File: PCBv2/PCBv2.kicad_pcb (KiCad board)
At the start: 2 copper layers, 150 x 110 mm, 76 parts, among them IC1 MAX743CWE+, J1 Arduino_Mega_Header, J10 Screw_Terminal_01x03, J11 Screw_Terminal_01x03, J12 Screw_Terminal_01x03, J13 Screw_Terminal_01x03, J2 Conn_01x10, J3 Conn_01x08, J4 Conn_01x08, J5 Conn_02x18_Odd_Even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

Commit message: Added photos of the prototype and changed the PCB
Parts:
- removed C20: 100nF, Cap:Cap
- moved C19 16.8 mm to (119.3, 144.0), turned to 270 degrees
- moved U3 14.9 mm to (173.1, 55.5)
- moved J13 14.6 mm to (213.8, 141.8)
- moved J12 14.5 mm to (213.8, 126.2)
- moved J11 14.4 mm to (213.8, 110.8)
- moved J10 14.4 mm to (213.7, 95.3)
- moved J9 14.2 mm to (213.7, 80.0)
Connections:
- C19 pad 2: /-15V -> /5V
- D5 pad 1: Net-(D5-Pad1) -> /5V
- R20 pad 2: Net-(D5-Pad1) -> /5V
- R21 pad 2: Net-(D5-Pad1) -> /5V
- U10 pad 4: /-15V -> /GND
- U10 pad 8: /+15V -> /5V
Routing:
- net /5V: track 205.5 -> 340.5 mm, vias 4 -> 7
- net /PIN50: track 192.9 -> 208.8 mm
- net /PIN53: track 25.2 -> 40.8 mm
- net /SMU2: track 102.7 -> 117.7 mm
- net /PIN51: track 23.7 -> 38.6 mm
- net /PIN52: track 186.8 -> 201.7 mm
- net /E-AMPLI: track 18.2 -> 33.0 mm
- net /E4: track 28.5 -> 43.1 mm
- net /E7: track 23.8 -> 38.4 mm
- net /SMU-IN: track 17.0 -> 31.5 mm
- net /E8: track 22.0 -> 36.5 mm
- net /E6: track 25.8 -> 40.3 mm
- net /E5: track 27.0 -> 41.5 mm
- net /ARDU-A11: track 103.4 -> 117.8 mm
- net /ARDU-A9: track 105.2 -> 119.5 mm
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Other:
- board size 150 x 110 mm -> 165.1 x 110 mm

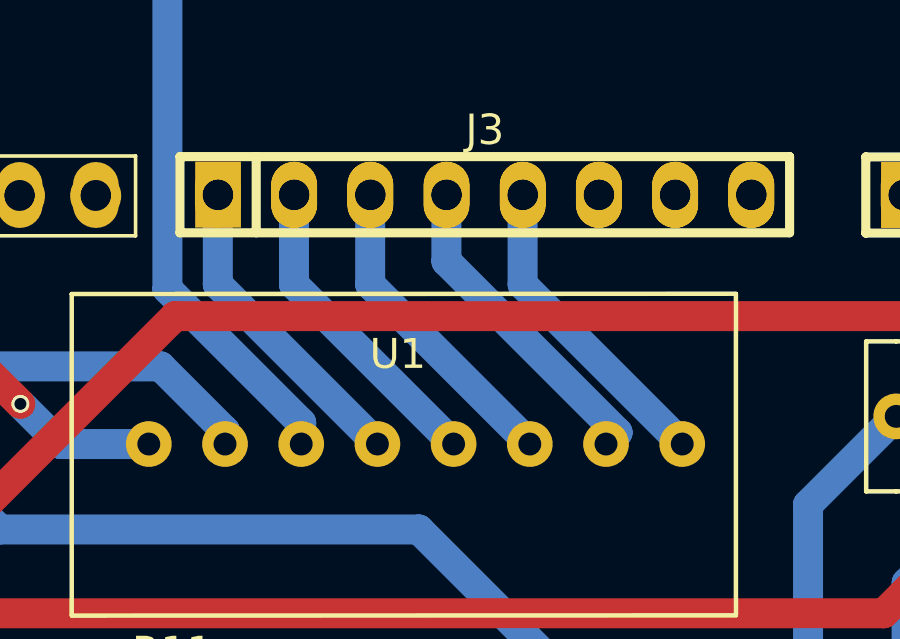
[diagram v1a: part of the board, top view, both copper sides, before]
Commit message: Changes on PCB and pins of LCD
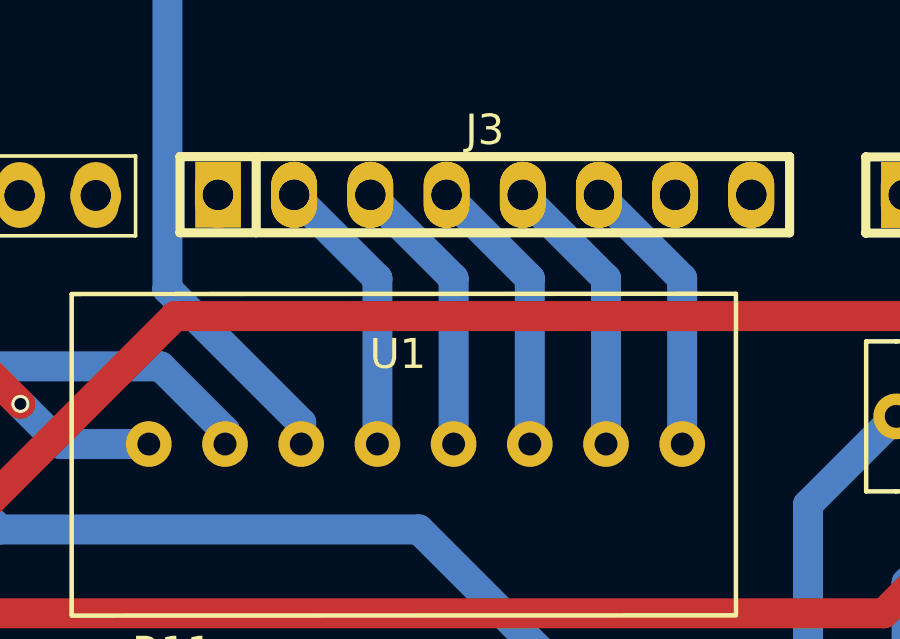
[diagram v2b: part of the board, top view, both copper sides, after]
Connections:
- J1 pad 71: Net-(J1-Pad71) -> /PIN2
- J1 pad 76: /PIN7 -> Net-(J1-Pad76)
- J3 pad 1: /PIN7 -> Net-(J3-Pad1)
- J3 pad 6: Net-(J3-Pad6) -> /PIN2
- U1 pad 1: /PIN3 -> /PIN2
- U1 pad 2: /PIN4 -> /PIN3
- U1 pad 3: /PIN5 -> /PIN4
- U1 pad 4: /PIN6 -> /PIN5
- U1 pad 5: /PIN7 -> /PIN6
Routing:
- net /PIN7: track 10.5 -> 0.00 mm
- net /PIN2: track 0.00 -> 9.45 mm
- net /PIN4: track 10.8 -> 9.45 mm
- net /PIN5: track 10.5 -> 9.45 mm
- net /PIN3: track 10.5 -> 9.45 mm
- net /PIN6: track 10.5 -> 9.45 mm

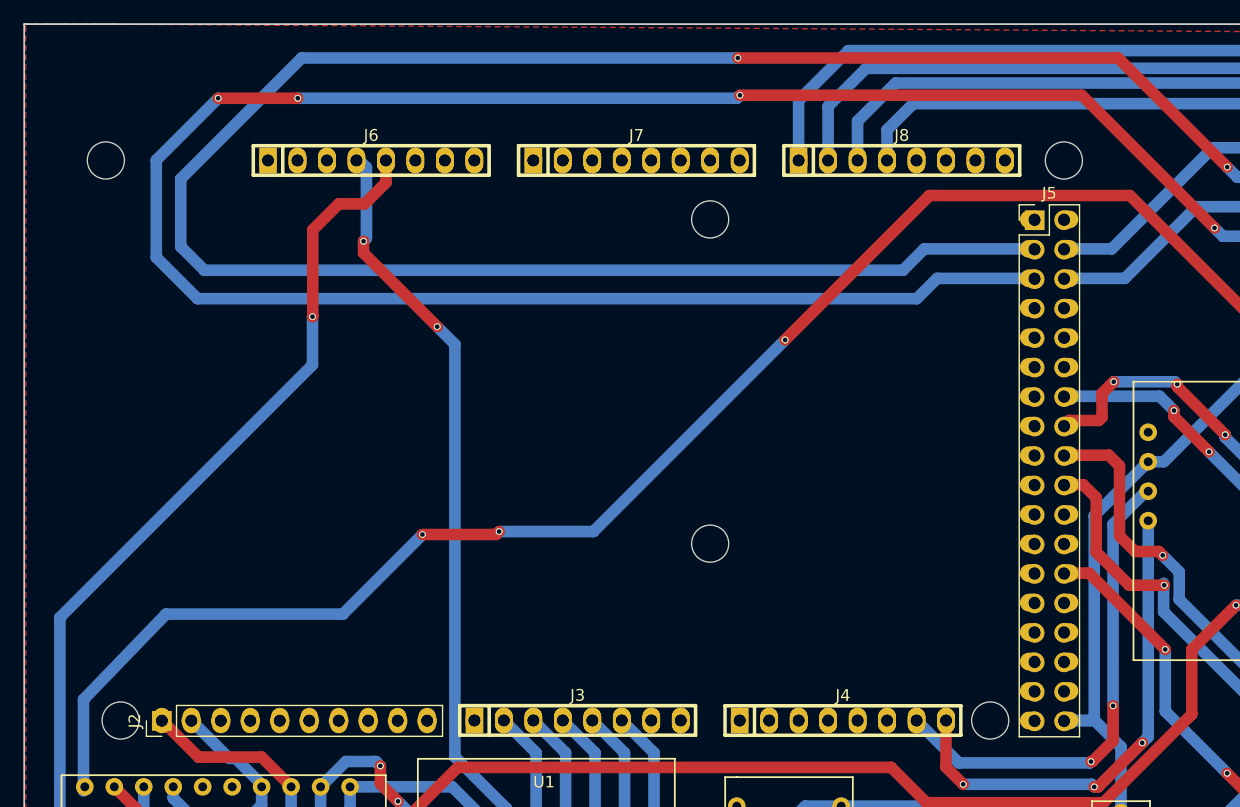
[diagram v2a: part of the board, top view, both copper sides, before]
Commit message: Added GPRS communications and lots of changes on the main code!
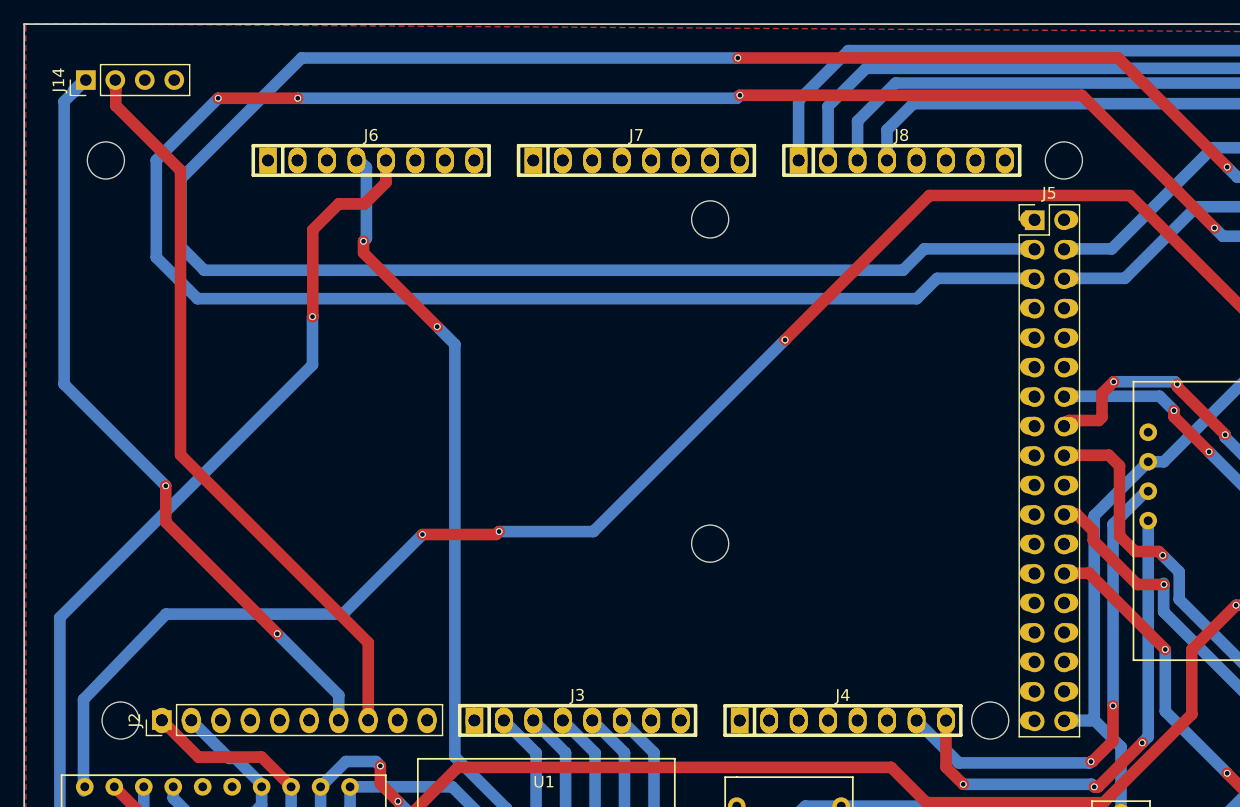
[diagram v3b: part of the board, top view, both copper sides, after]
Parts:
- added J14: Conn_01x04, Pin_Headers:Pin_Header_Straight_1x04_Pitch2.54mm, F.Cu at (55.3, 54.8)
- moved J2 0.07 mm to (61.9, 110.0)
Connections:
- J1 pad 52: /PIN37 -> Net-(J1-Pad52)
- J1 pad 53: Net-(J1-Pad53) -> /PIN35
- J1 pad 79: Net-(J1-Pad79) -> /PIN10
- J1 pad 80: Net-(J1-Pad80) -> /PIN11
- J2 pad 7: Net-(J2-Pad7) -> /PIN11
- J2 pad 8: Net-(J2-Pad8) -> /PIN10
- J5 pad 20: /PIN37 -> Net-(J5-Pad20)
- J5 pad 22: Net-(J5-Pad22) -> /PIN35
- U4 pad 2: /PIN37 -> /PIN35
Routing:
- net /PIN11: track 0.00 -> 67.4 mm, vias 0 -> 2
- net /PIN10: track 0.00 -> 65.8 mm
- net /PIN37: track 41.3 -> 0.00 mm, vias 3 -> 0
- net /PIN35: track 0.00 -> 38.7 mm, vias 0 -> 3

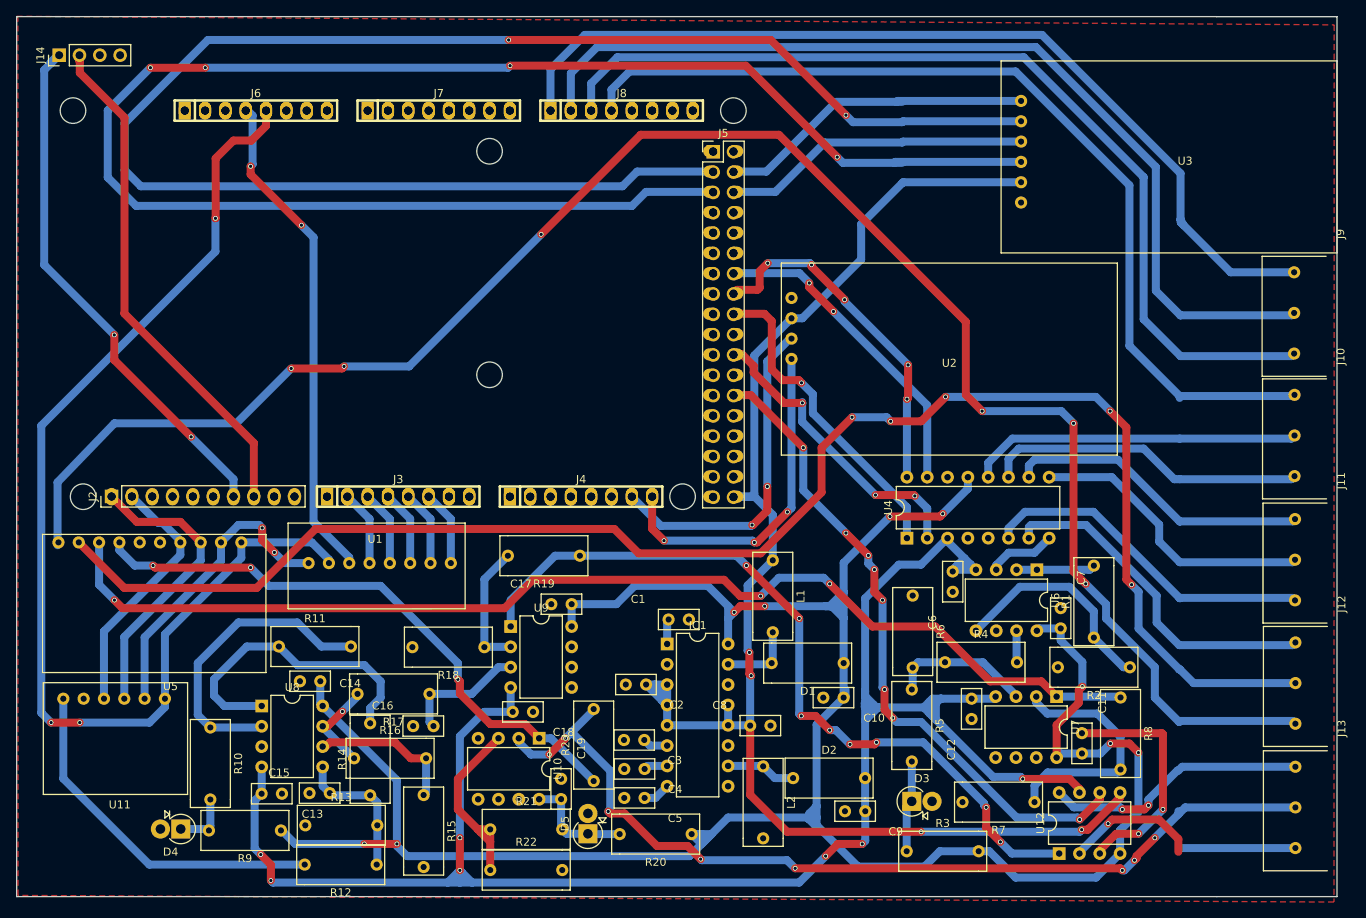
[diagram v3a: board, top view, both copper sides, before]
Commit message: Added pwr pin of the SIM900 and documentation made
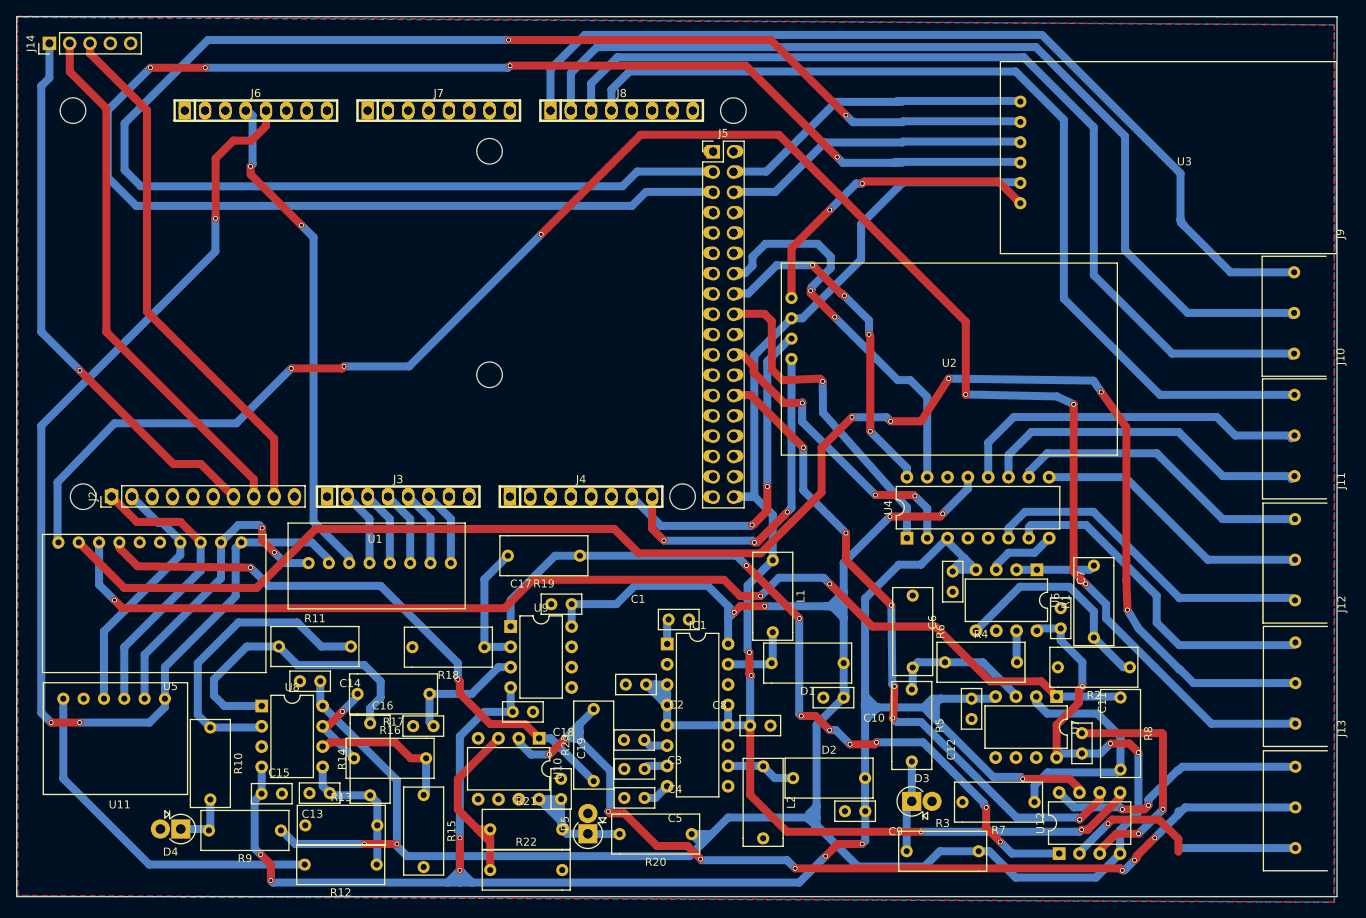
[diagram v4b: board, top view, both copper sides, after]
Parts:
- J14: value Conn_01x04 -> Conn_01x05; footprint Pin_Headers:Pin_Header_Straight_1x04_Pitch2.54mm -> Pin_Headers:Pin_Header_Straight_1x05_Pitch2.54mm
- moved J14 1.92 mm to (54.1, 53.3)
- moved U3 0.12 mm to (173.0, 55.6)
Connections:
- J1 pad 78: Net-(J1-Pad78) -> /PIN9
- J14 pad 3: /GND -> /PIN9
- J2 pad 9: Net-(J2-Pad9) -> /PIN9
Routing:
- net /PIN9: track 0.00 -> 66.2 mm
- net /GND: track 68.2 -> 107.6 mm, vias 4 -> 6
- net /PIN43: track 40.4 -> 50.6 mm
- net /5V: track 340.5 -> 347.5 mm
- net /SMU2: track 117.7 -> 122.2 mm
- net /E5: track 41.5 -> 45.4 mm
- net /ADC-A2: track 199.2 -> 202.1 mm
- net /E6: track 40.3 -> 42.6 mm
- net /PIN11: track 67.4 -> 69.1 mm, vias 2 -> 1
- net /PIN41: track 44.2 -> 42.8 mm, vias 5 -> 4
- net /PIN39: track 40.5 -> 41.9 mm
- net /ARDU-A11: track 117.8 -> 119.0 mm
- net /E8: track 36.5 -> 35.5 mm
- net /ADC-A3: track 230.8 -> 230.1 mm
- net /ARDU-A10: track 118.6 -> 119.2 mm
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- added copper zone on B.Cu, net /GND

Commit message: Changes on PCB track width and small track changes
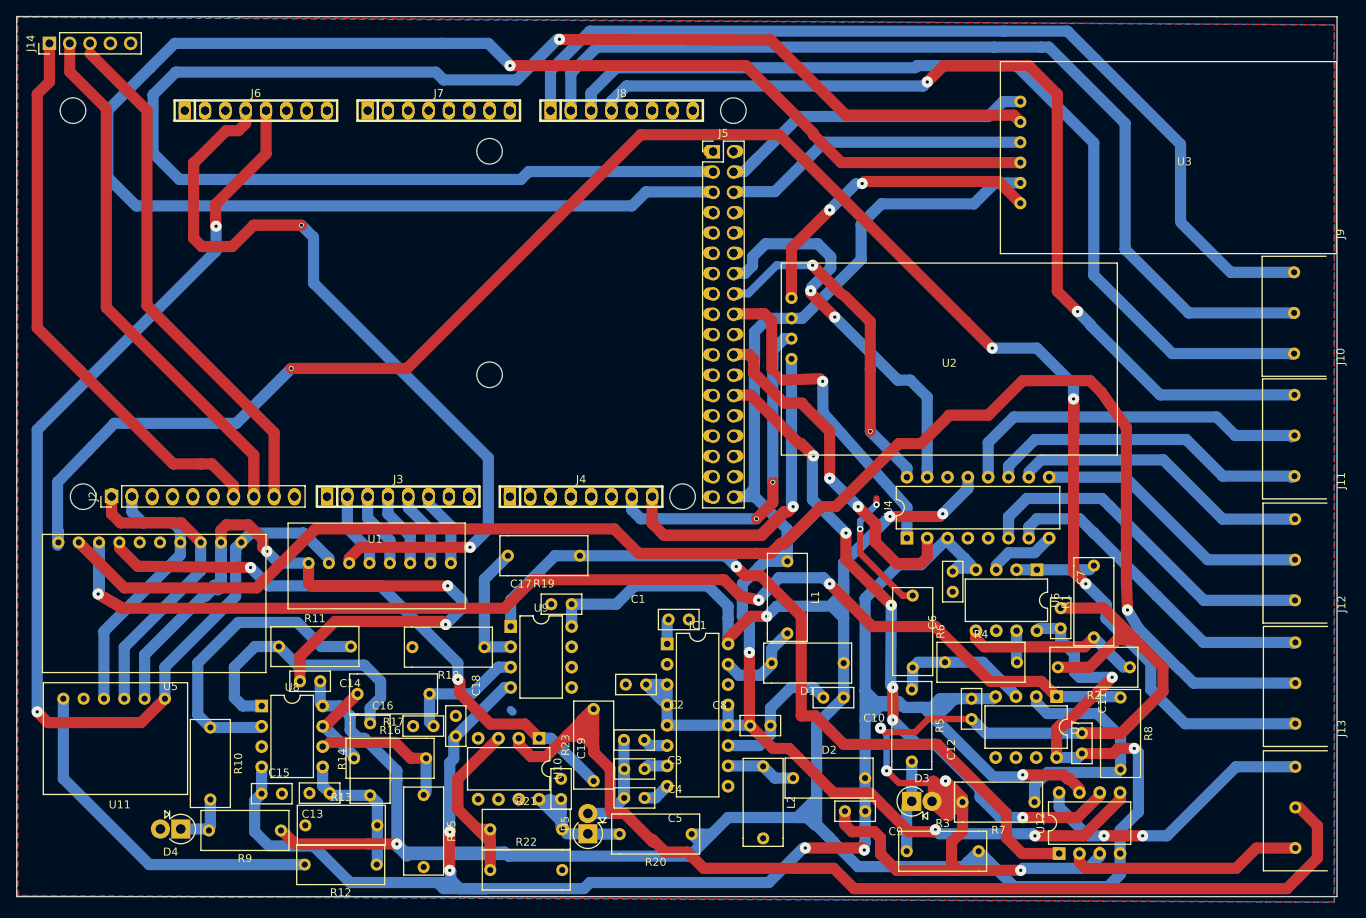
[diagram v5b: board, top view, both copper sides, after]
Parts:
- moved C18 9.86 mm to (106.2, 136.1), turned to 270 degrees
- moved L1 1.83 mm to (148.8, 117.1)
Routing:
- net /GND: track 107.6 -> 352.9 mm, vias 6 -> 11
- net /+15V: track 305.4 -> 381.0 mm, vias 9 -> 6
- net /SMU2: track 122.2 -> 164.3 mm, vias 8 -> 0
- net /3.3V: track 62.3 -> 102.0 mm
- net /-15V: track 237.6 -> 276.8 mm, vias 7 -> 5
- net /SCL: track 79.6 -> 98.9 mm, vias 3 -> 1
- net /5V: track 347.5 -> 365.2 mm, vias 7 -> 5
- net /VO-REDU: track 143.7 -> 154.6 mm
- net /PIN35: track 38.7 -> 45.5 mm, vias 3 -> 2
- net Net-(R16-Pad1): track 11.8 -> 17.5 mm, vias 1 -> 0
- net /ADC-A3: track 230.1 -> 235.7 mm, vias 6 -> 4
- net /PIN52: track 201.7 -> 196.6 mm, vias 2 -> 1
- net Net-(R1-Pad1): track 27.6 -> 22.8 mm
- net Net-(R11-Pad1): track 38.6 -> 34.6 mm
- net /PIN53: track 40.8 -> 44.8 mm
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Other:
- net class Default: trace_width 1 -> 1.4; via_dia 0.6 -> 1.4

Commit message: Added output via terminal and voltage sweep for I/V curves with the SMU
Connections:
- IC1 pad 9: Net-(IC1-Pad9) -> /-15V
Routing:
- net /-15V: track 276.8 -> 294.1 mm, vias 5 -> 6
- net Net-(R4-Pad2): track 3.96 -> 6.50 mm
